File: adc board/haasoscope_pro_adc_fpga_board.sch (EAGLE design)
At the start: 614 parts, among them CN2 12Vin, IC1 ADC12DL2500ACF, IC10 TPS72325DBVR, IC13 LMH5401IRMST, IC14 LMH6401IRMZR, IC15 SN74AVC4T774PWR, IC17 DAC8562SDGSR, IC18 TLV9102IPWR, IC2 SN74AVC4T774PWR, IC21 LMH5401IRMST, IC22 TPS7A7200RGTR, IC23 TPS7A7200RGTR, IC24 TPS7A7200RGTR, IC25 TPS72325DBVR, IC26 TPS7A7200RGTR, IC27 TPS7A7200RGTR, IC28 TPS7A7200RGTR, IC29 LMH6401IRMZR, IC3 ADC122S021CIMM_NOPB, IC30 SN74AVC4T774PWR, IC33 TLV9102IPWR, IC4 TLV9102IPWR, IC5 EP4CE30F23C6N, IC6 EPCQ16ASI8N, IC7 TPS7A7200RGTR, IC8 FT232HQ, IC9 93LC56B, J1 2p-2.54, J11 8pin, J15 test1, J2 test1, J3 2p-2.54, J30 2p-2.54, J31 2p-2.54, J32 2p-2.54, J33 2p-2.54, J34 2p-2.54, J35 2p-2.54, J36 2p-2.54, J37 2p-2.54, J39 2p-2.54, J4 2p-2.54, J40 2p-2.54, J41 2p-2.54, J42 2p-2.54, J43 2p-2.54, J44 2p-2.54, J45 2p-2.54, J46 2p-2.54, J5 1x4, K1 G6K-2F-RF-T-TR03_DC5, K2 G6K-2F-RF-T-TR03_DC5, K3 G6K-2F-RF-T-TR03_DC5, K4 G6K-2F-RF-T-TR03_DC5, K5 G6K-2F-RF-T-TR03_DC5, K6 TLP3475_TP,F, K7 TLP3475_TP,F, Q1 S8050, Q2 FDN340P, Q4 S8050, Q5 S8050, Q7 S8050, Q8 S8050, Q9 S8050, SW3 SKQGADE010, SW4 SKQGADE010, U2 ADF4350BCPZ, X1 USBC, Y2 OSCILLATORSMD-5X3, Y3 12MHz

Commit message: cleaned up schematics a little
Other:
- note added: "Connect USB-C power to 5V only if 12V not connected If 12VConnected is high (5V), then switch is off If 12VConnected is low (0V), then switch is on"
- note added: "From USB-C"
- note added: "To FPGA to see if 12V connected. Open-drain, so have to pull up to 2V5."
- note removed: "Connect USBC power to 5V only if 12V not connected (detected by power jack on next sheet) If 12VConnected is high (5V), then switch is off If 12VConnected is low (0V), then switch is on"
- note removed: "To FPGA to see if 12V connected"
- moved on the sheet: C138, C139, C140, C141, C243, C287, C289, C290, C291, C292, C293, C321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

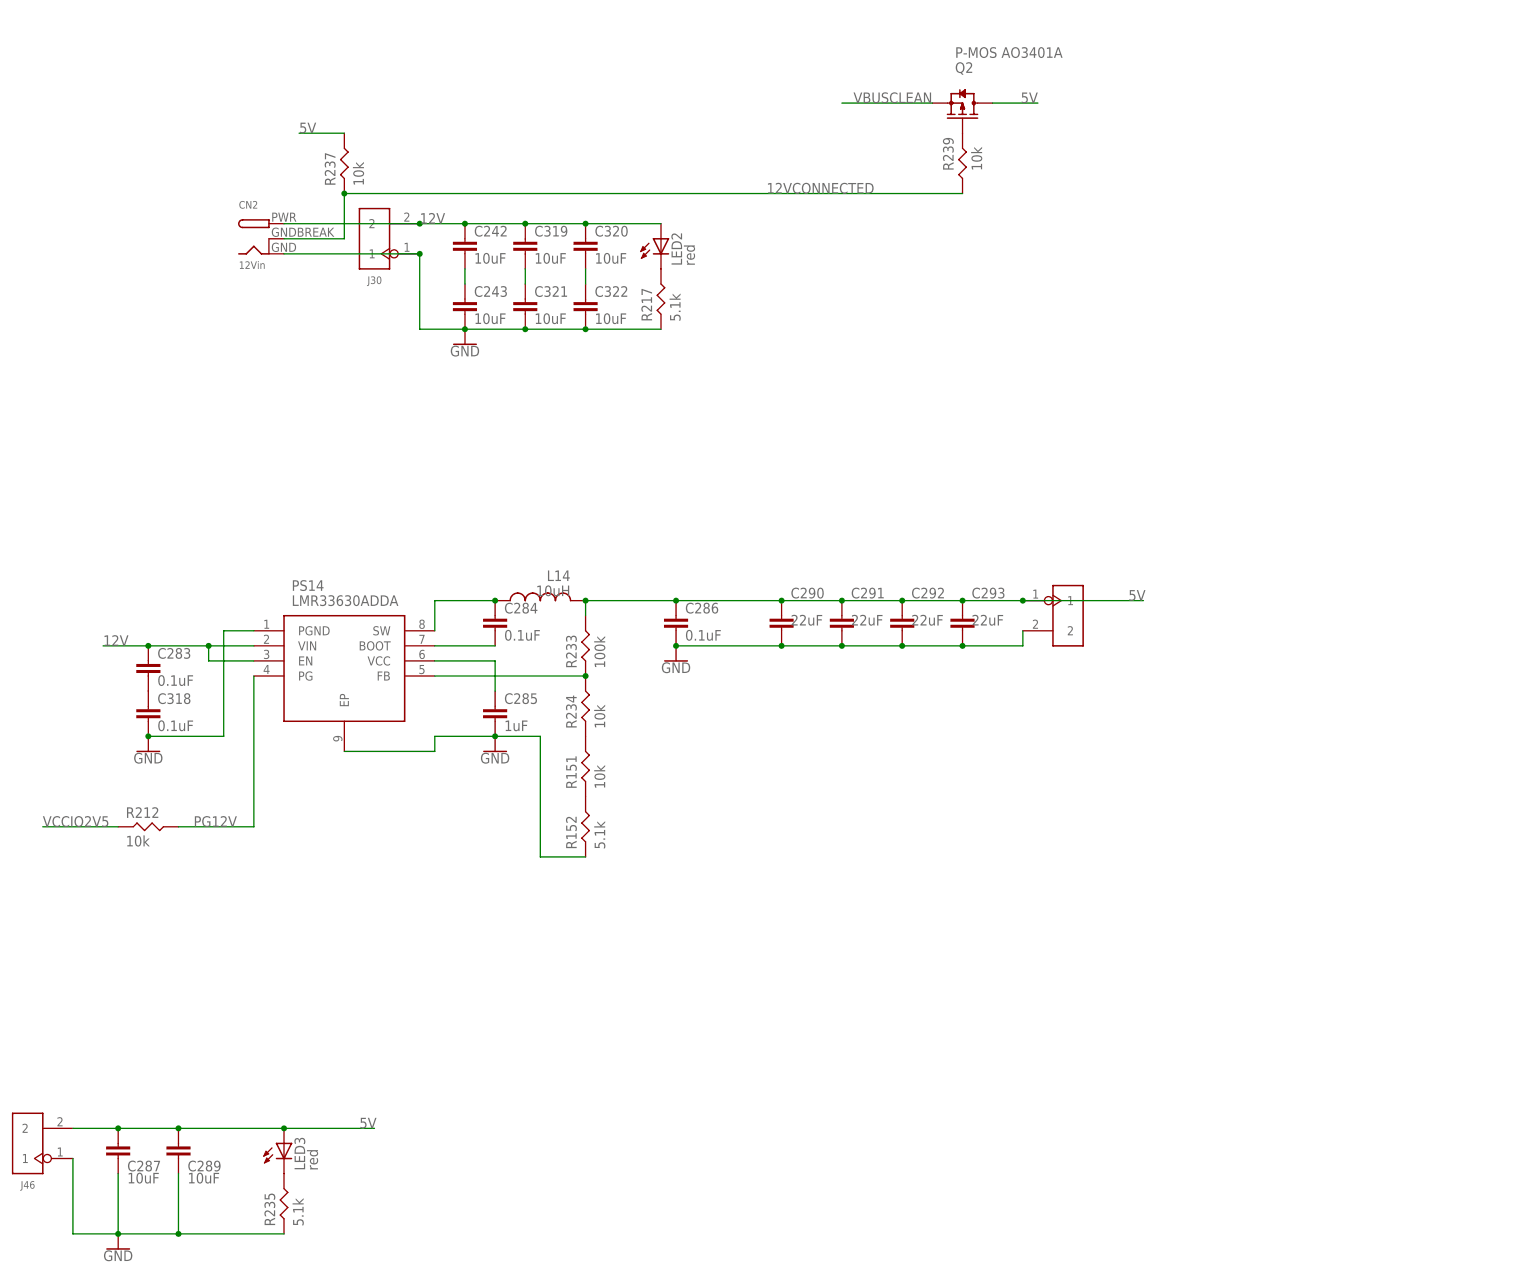
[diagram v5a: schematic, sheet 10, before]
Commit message: add much more filtering of 5V input
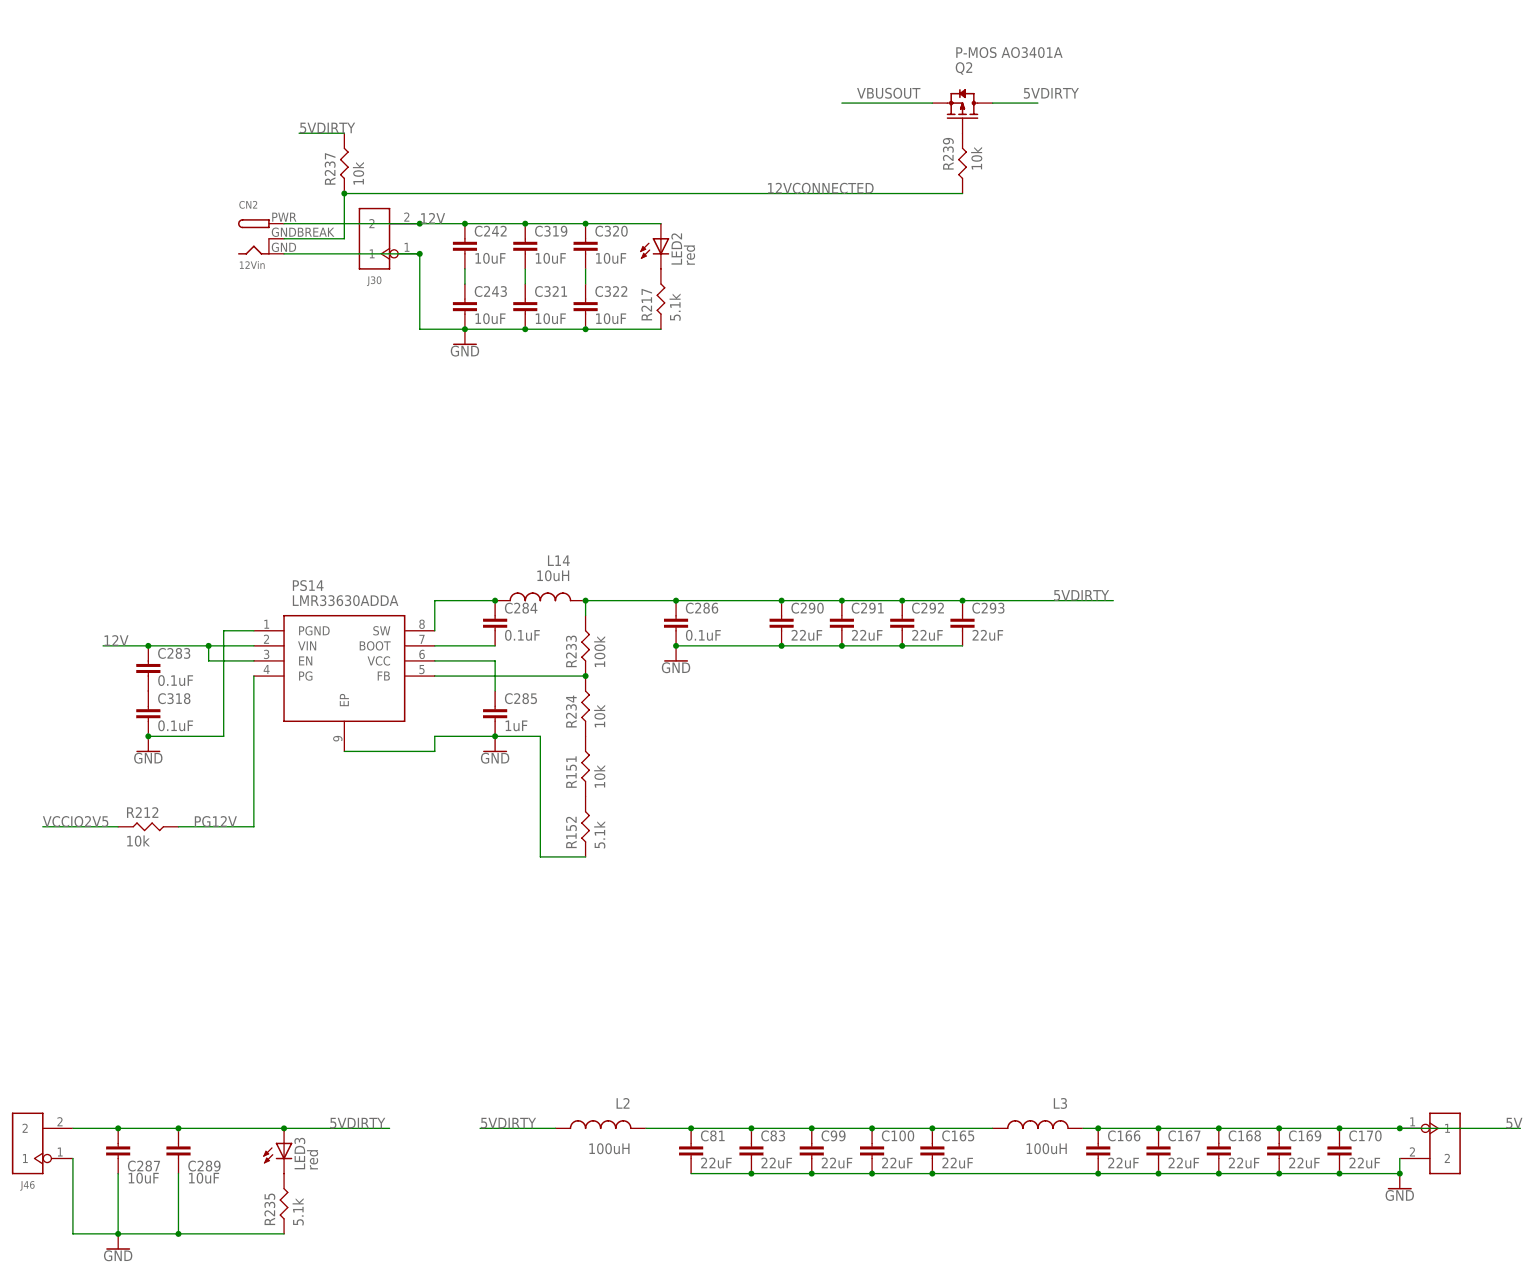
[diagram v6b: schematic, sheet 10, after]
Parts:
- added C100, C165, C166, C167, C168, C169, C170, C81, C83, C99: 22uF, Nordic_nRF:CAPACITOR_0805_N
- added L2, L3: 100uH, SparkFun-Passives:INDUCTORPWR
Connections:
- net VBUSCLEAN renamed VBUSOUT
- new net 5VDIRTY: C286.1, C287.1, C289.1, C290.1, C291.1, C292.1, C293.1, J46.2, L14.2, L2.1, LED3.A, Q2.D, R233.P$2, R237.P$2
- new net 5VDIRTYT: C100.1, C165.1, C81.1, C83.1, C99.1, L2.2, L3.1
- net 5V: now also C166.1, C167.1, C168.1, C169.1, C170.1, L3.2; no longer C286.1, C287.1, C289.1, C290.1, C291.1, C292.1, C293.1, J46.2, L14.2, LED3.A, Q2.D, R233.P$2, R237.P$2
- net GND: now also C100.2, C165.2, C166.2, C167.2, C168.2, C169.2, C170.2, C81.2, C83.2, C99.2
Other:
- note added: "Filter the incoming 5V heavily - the USB power may be very noisy"

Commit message: use 1000 uF caps
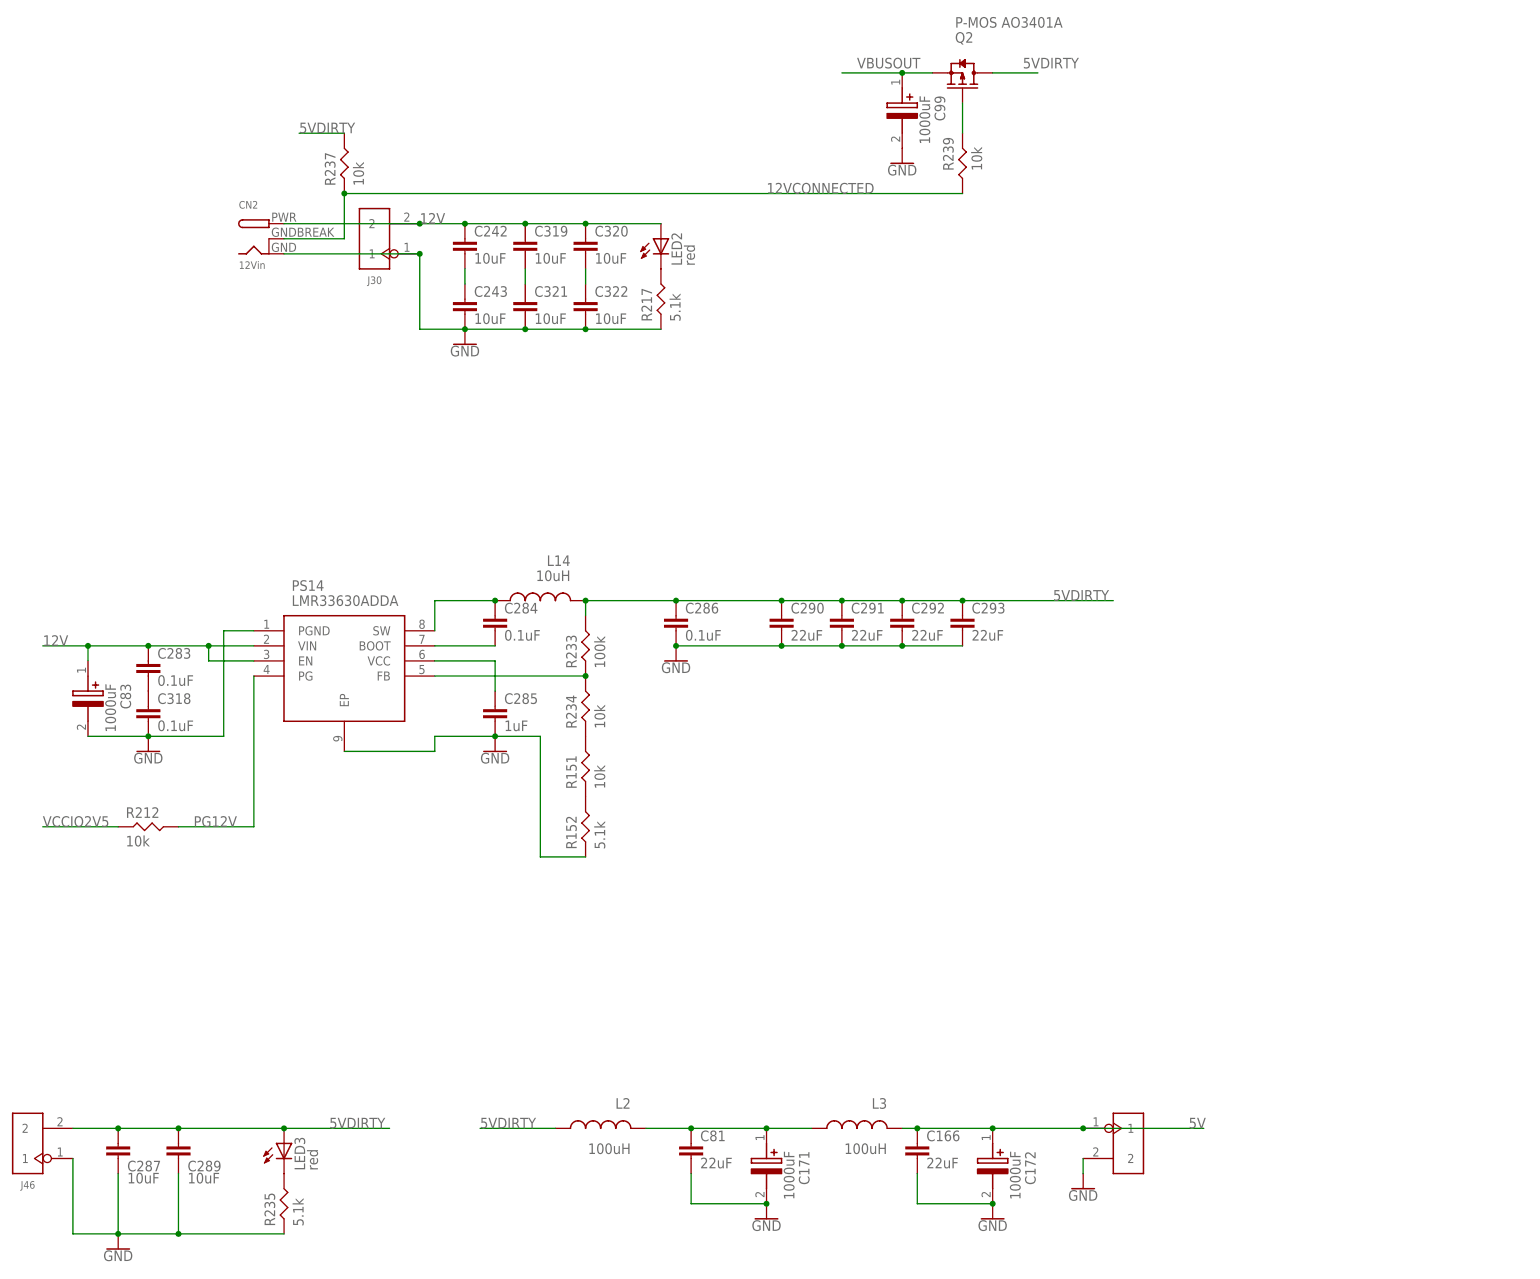
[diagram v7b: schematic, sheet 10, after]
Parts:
- removed C100, C165, C167, C168, C169, C170: 22uF, Nordic_nRF:CAPACITOR_0805_N
- added C171, C172: 1000uF, EEE-FT1E102UP:EEE-FT1E102UP
- C83, C99: value 22uF -> 1000uF; device Nordic_nRF:CAPACITOR_0805_N -> EEE-FT1E102UP:EEE-FT1E102UP; LCSC (none) -> C401766
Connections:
- net 12V: now also C83.+
- net 5V: now also C172.+; no longer C167.1, C168.1, C169.1, C170.1
- net 5VDIRTYT: now also C171.+; no longer C100.1, C165.1, C83.1, C99.1
- net GND: now also C171.-, C172.-, C83.-, C99.-; no longer C100.2, C165.2, C167.2, C168.2, C169.2, C170.2, C83.2, C99.2
- net VBUSOUT: now also C99.+
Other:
- moved on the sheet: C166, L3, Q2
